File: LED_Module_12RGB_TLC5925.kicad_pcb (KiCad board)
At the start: 2 copper layers, 41.8 x 33.3 mm, 18 parts, among them U1 TLC5925IPWR

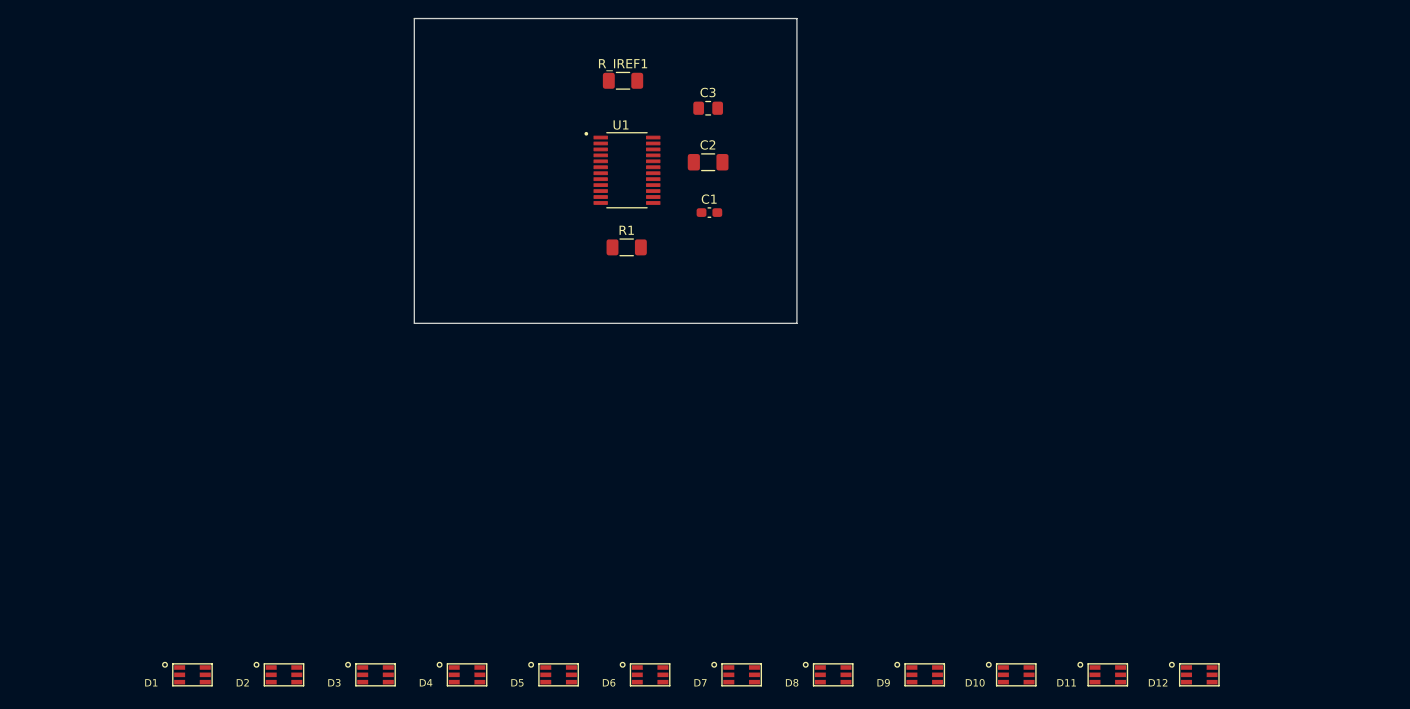
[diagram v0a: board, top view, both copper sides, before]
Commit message: v0 2 layer needs grounding islands
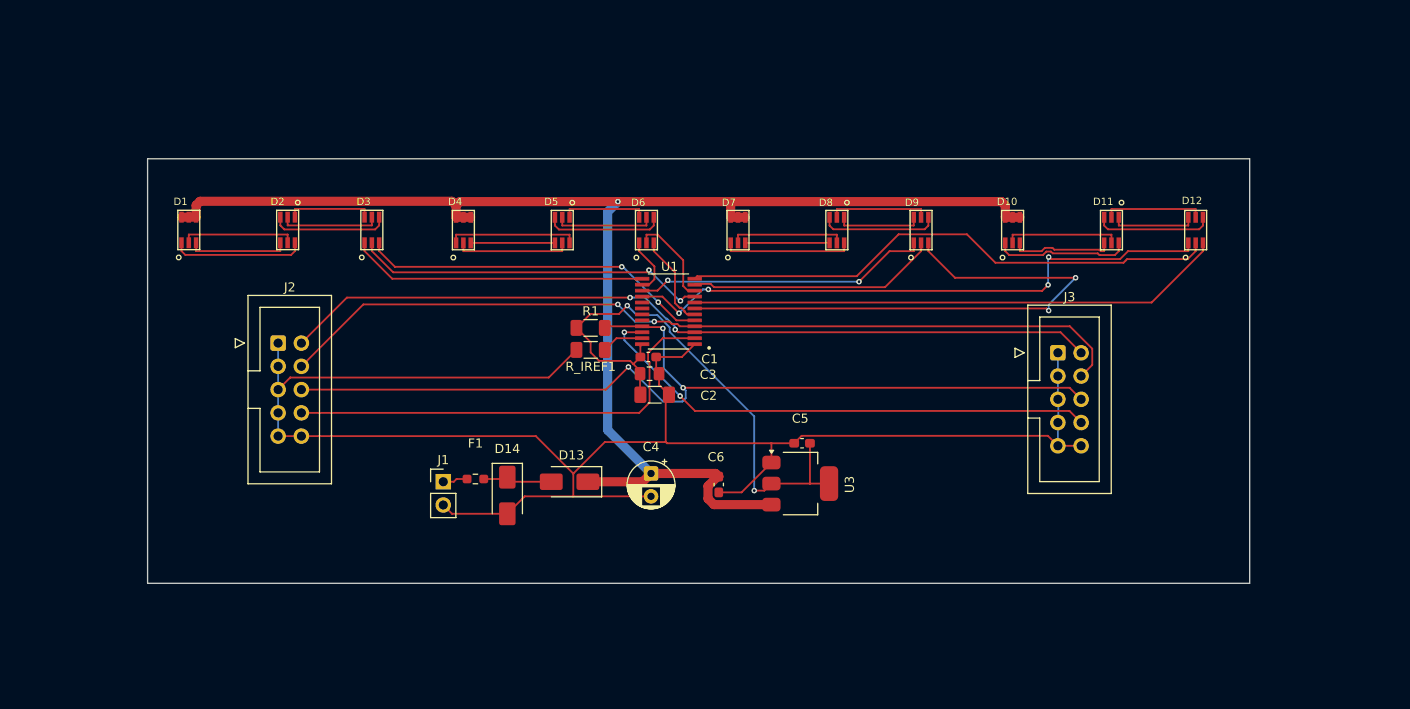
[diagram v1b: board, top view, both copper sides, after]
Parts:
- added C4: 100uF, Capacitor_THT:CP_Radial_D5.0mm_P2.50mm, F.Cu at (129.1, 102.6)
- added C5: 0.1uF, Capacitor_SMD:C_0603_1608Metric_Pad1.08x0.95mm_HandSolder, F.Cu at (145.6, 99.3)
- added C6: 0.1uF, Capacitor_SMD:C_0603_1608Metric_Pad1.08x0.95mm_HandSolder, F.Cu at (136.5, 103.8)
- added D13: SS34, Diode_SMD:D_SMA, F.Cu at (120.2, 103.5)
- added D14: SMAJ15A, Diode_SMD:D_SMA, F.Cu at (113.4, 105.0)
- added F1: 1A, Resistor_SMD:R_0603_1608Metric_Pad0.98x0.95mm_HandSolder, F.Cu at (109.9, 103.2)
- added J1: Conn_01x02_Pin, Connector_PinHeader_2.54mm:PinHeader_1x02_P2.54mm_Vertical, F.Cu at (106.4, 103.5)
- added J2: Conn_02x05_Counter_Clockwise, Connector_IDC:IDC-Header_2x05_P2.54mm_Vertical, F.Cu at (88.4, 88.4)
- added J3: Conn_02x05_Counter_Clockwise, Connector_IDC:IDC-Header_2x05_P2.54mm_Vertical, F.Cu at (173.5, 89.4)
- added U3: AMS1117-3.3, Package_TO_SOT_SMD:SOT-223-3_TabPin2, F.Cu at (145.4, 103.7)
- moved D1 49.0 mm to (79.0, 76.0), turned to 90 degrees
- moved D2 49.0 mm to (89.0, 76.0), turned to -90 degrees
- moved D3 49.0 mm to (99.0, 76.0), turned to 90 degrees
- moved D10 49.0 mm to (169.0, 76.0), turned to 90 degrees
- moved D11 49.0 mm to (179.0, 76.0), turned to -90 degrees
- moved D12 49.0 mm to (189.0, 76.0), turned to 90 degrees
- moved D4 49.0 mm to (109.0, 76.0), turned to 90 degrees
- moved D5 49.0 mm to (119.0, 76.0), turned to -90 degrees
- moved D6 49.0 mm to (129.0, 76.0), turned to 90 degrees
- moved D7 49.0 mm to (139.0, 76.0), turned to 90 degrees
- moved D8 49.0 mm to (149.0, 76.0), turned to -90 degrees
- moved D9 49.0 mm to (159.0, 76.0), turned to 90 degrees
- moved C3 29.7 mm to (128.9, 91.7)
- moved R_IREF1 29.6 mm to (122.5, 89.1), turned to 180 degrees
- moved C2 26.1 mm to (129.5, 94.0)
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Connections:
- net Net-(U1-~{OE}) renamed OE
- U1 pad 2: unconnected-(U1-SDI-Pad2) -> SDI
- U1 pad 22: unconnected-(U1-SDO-Pad22) -> SDO
- U1 pad 3: unconnected-(U1-CLK-Pad3) -> CLK
- U1 pad 4: unconnected-(U1-LE-Pad4) -> LE
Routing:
- net GND: track 0.00 -> 194.3 mm
- net +12V: track 0.00 -> 158.2 mm, vias 0 -> 1
- net OE: track 0.00 -> 104.3 mm, vias 0 -> 3
- net LE: track 0.00 -> 94.7 mm, vias 0 -> 2
- net CLK: track 0.00 -> 89.9 mm, vias 0 -> 2
- net OUT11_B3: track 0.00 -> 66.2 mm, vias 0 -> 4
- net OUT2_R2: track 0.00 -> 61.8 mm, vias 0 -> 2
- net VDD_3V3: track 0.00 -> 61.6 mm, vias 0 -> 2
- net OUT7_G3: track 0.00 -> 59.5 mm
- net OUT3_R3: track 0.00 -> 58.8 mm
- net SDO: track 0.00 -> 56.4 mm, vias 0 -> 2
- net SDI: track 0.00 -> 49.8 mm
- net OUT4_G0: track 0.00 -> 38.8 mm, vias 0 -> 2
- net OUT0_R0: track 0.00 -> 38.5 mm, vias 0 -> 2
- net OUT8_B0: track 0.00 -> 32.5 mm
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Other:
- board size 41.8 x 33.3 mm -> 120.4 x 46.4 mm

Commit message: v1 ok
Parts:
- added H1: 3.2mm_M3, footprints:MountingHole_3.2mm_M3, F.Cu at (66.5, 78.5)
- added H2: 3.2mm_M3, footprints:MountingHole_3.2mm_M3, F.Cu at (203.5, 78.5)
- added H3: 3.2mm_M3, footprints:MountingHole_3.2mm_M3, F.Cu at (203.5, 107.5)
- added H4: 3.2mm_M3, footprints:MountingHole_3.2mm_M3, F.Cu at (66.4, 107.5)
- added R2: 330, Resistor_SMD:R_1206_3216Metric_Pad1.30x1.75mm_HandSolder, F.Cu at (156.0, 103.6)
- C4, J1, J2, J3: moved to B.Cu
- moved D14 12.8 mm to (126.1, 106.7)
- moved J2 5.69 mm to (93.8, 89.9), turned to 180 degrees
- moved J3 5.66 mm to (179.0, 90.9), turned to 180 degrees
- moved C2 3.30 mm to (132.4, 95.5)
- moved C4 3.30 mm to (132.0, 104.1)
- moved C5 3.30 mm to (148.5, 100.8)
- moved C6 3.30 mm to (139.4, 105.3)
- moved D1 3.30 mm to (81.9, 77.5)
- moved D2 3.30 mm to (91.9, 77.5)
- moved D3 3.30 mm to (101.9, 77.5)
- moved R_IREF1 3.30 mm to (125.4, 90.6)
- moved C3 3.30 mm to (131.9, 93.2)
- moved D10 3.30 mm to (171.9, 77.5)
- moved D11 3.30 mm to (181.9, 77.5)
- moved D12 3.30 mm to (191.9, 77.5)
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- renumbered U3 to U2
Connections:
- D14 pad 1: Net-(D13-A) -> +12V
- J2 pad 1: GND -> CLK
- J2 pad 2: CLK -> GND
- J2 pad 3: GND -> LE
- J2 pad 4: LE -> GND
- J2 pad 5: GND -> OE
- J2 pad 6: OE -> GND
- J2 pad 7: GND -> SDI
- J2 pad 8: SDI -> GND
- J3 pad 1: GND -> CLK
- J3 pad 2: CLK -> GND
- J3 pad 3: GND -> LE
- J3 pad 4: LE -> GND
- J3 pad 5: GND -> OE
- J3 pad 6: OE -> GND
- J3 pad 7: GND -> SDO
- J3 pad 8: SDO -> GND
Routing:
- net GND: track 194.3 -> 10.9 mm, vias 0 -> 23
- net SDI: track 49.8 -> 5.98 mm, vias 0 -> 4
- net +12V: track 158.2 -> 118.8 mm, vias 1 -> 0
- net Net-(D13-A): track 7.66 -> 0.00 mm
- net /Connectors/12V IN: track 2.72 -> 0.00 mm
- net LE: track 94.7 -> 96.0 mm
- net CLK: track 89.9 -> 89.0 mm
- net VDD_3V3: track 61.6 -> 60.8 mm, vias 2 -> 0
- net OE: track 104.3 -> 104.8 mm
- added copper zone on B.Cu, net GND
- added copper zone on F.Cu, net GND
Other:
- board size 120.4 x 46.4 mm -> 150 x 42 mm
- board text added: "+12V"
- board text added: "CLK"
- board text added: "GND"
- board text added: "IN"
- board text added: "LE"
- board text added: "OE"
- board text added: "OUT"
- board text added: "POWER"
- board text added: "SDI"
- board text added: "SDO"

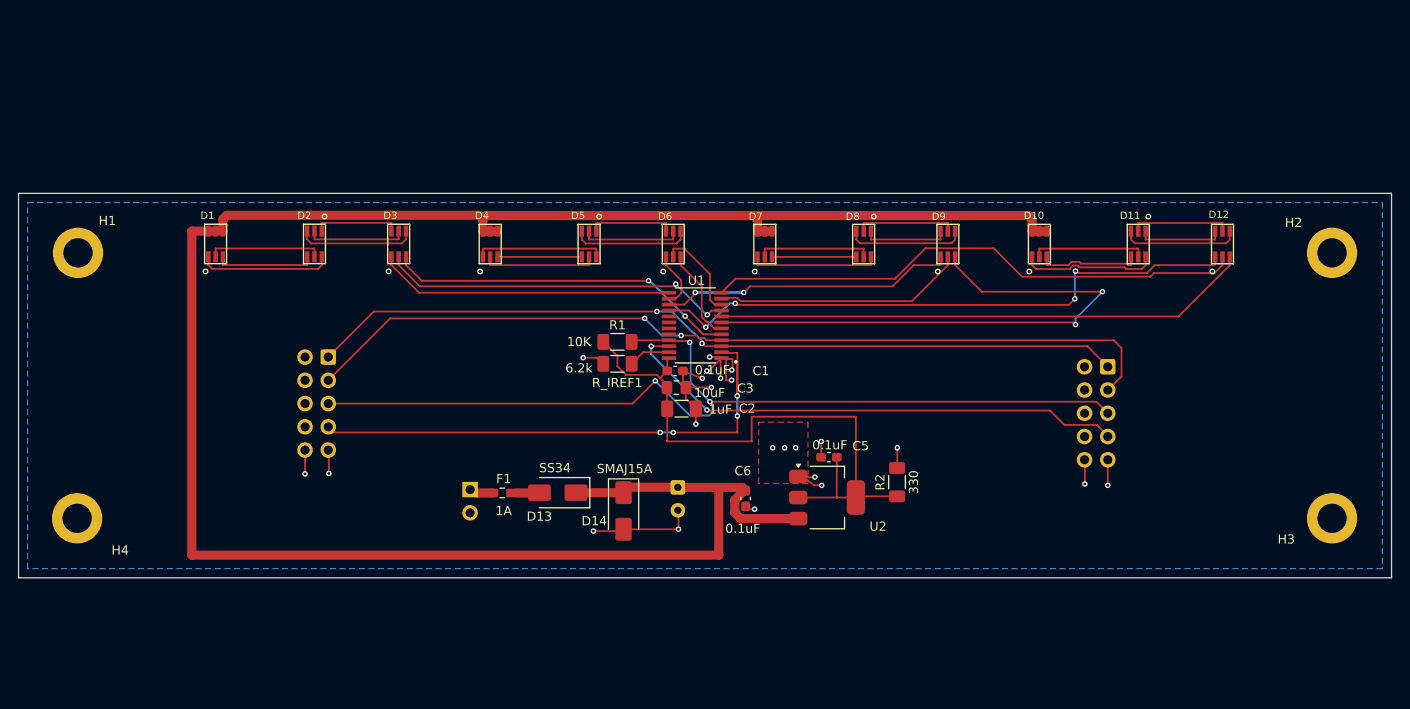
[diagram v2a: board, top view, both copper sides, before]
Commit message: LEDs P10 distance fix
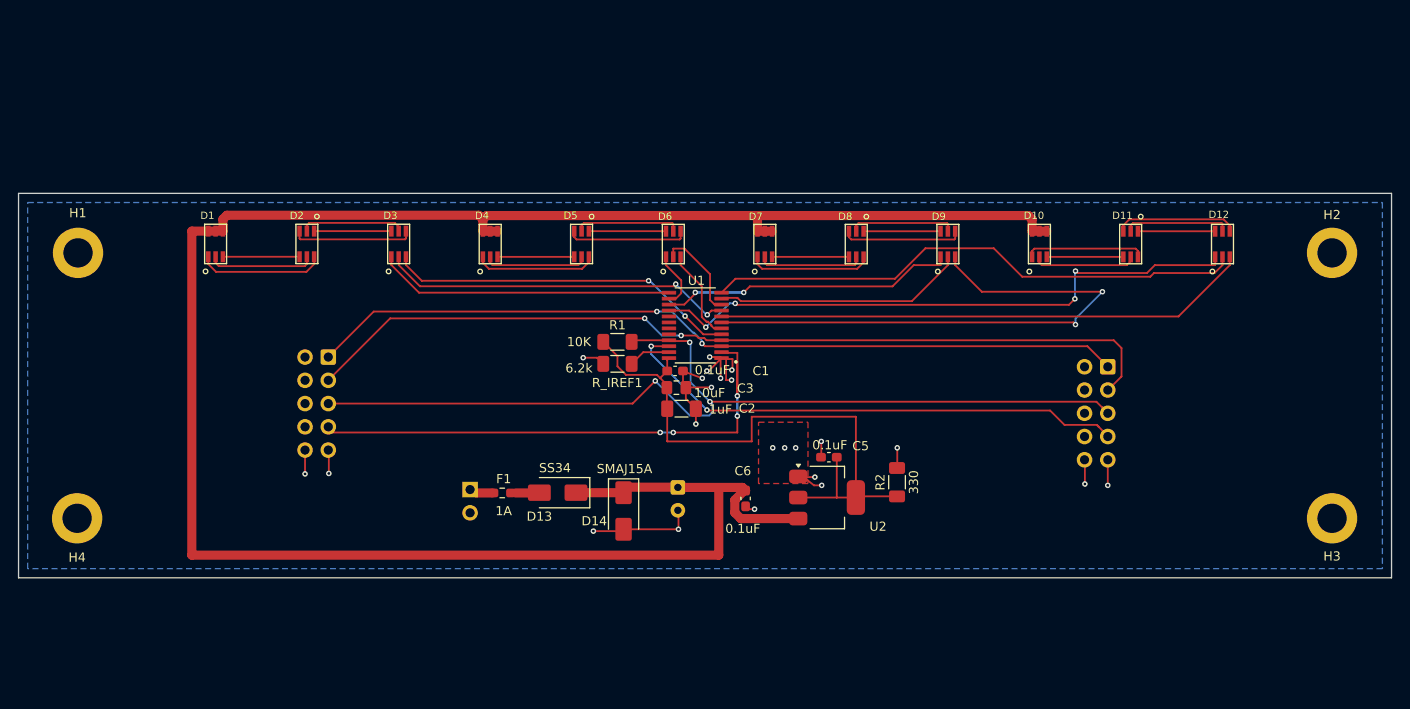
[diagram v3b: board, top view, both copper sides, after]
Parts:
- H1, H2, H3, H4: footprint footprints:MountingHole_3.2mm_M3 -> Mounting Hole:3.2mm_M3_TH
- moved D11 0.83 mm to (181.1, 77.5)
- moved D2 0.83 mm to (91.1, 77.5)
- moved D5 0.82 mm to (121.1, 77.5)
- moved D8 0.81 mm to (151.1, 77.5)
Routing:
- net Net-(D10-R_C): track 11.3 -> 8.37 mm
- net Net-(D1-R_C): track 11.0 -> 8.37 mm
- net Net-(D10-B_C): track 14.9 -> 13.1 mm
- net Net-(D10-G_C): track 12.6 -> 10.9 mm
- net Net-(D4-G_C): track 12.6 -> 11.4 mm
- net Net-(D7-G_C): track 12.6 -> 11.6 mm
- net Net-(D8-B_C): track 9.40 -> 8.41 mm
- net Net-(D5-B_C): track 9.40 -> 8.41 mm
- net Net-(D11-B_C): track 9.40 -> 8.43 mm
- net Net-(D2-B_C): track 9.40 -> 8.43 mm
- net Net-(D1-G_C): track 12.6 -> 11.7 mm
- net Net-(D4-B_C): track 14.2 -> 13.4 mm
- net Net-(D4-R_C): track 9.20 -> 8.37 mm
- net Net-(D7-R_C): track 9.20 -> 8.39 mm
- net Net-(D7-B_C): track 14.2 -> 13.5 mm
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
